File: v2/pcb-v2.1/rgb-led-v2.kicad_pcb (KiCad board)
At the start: 2 copper layers, 90 x 50 mm, 12 parts, among them SW1 SPST

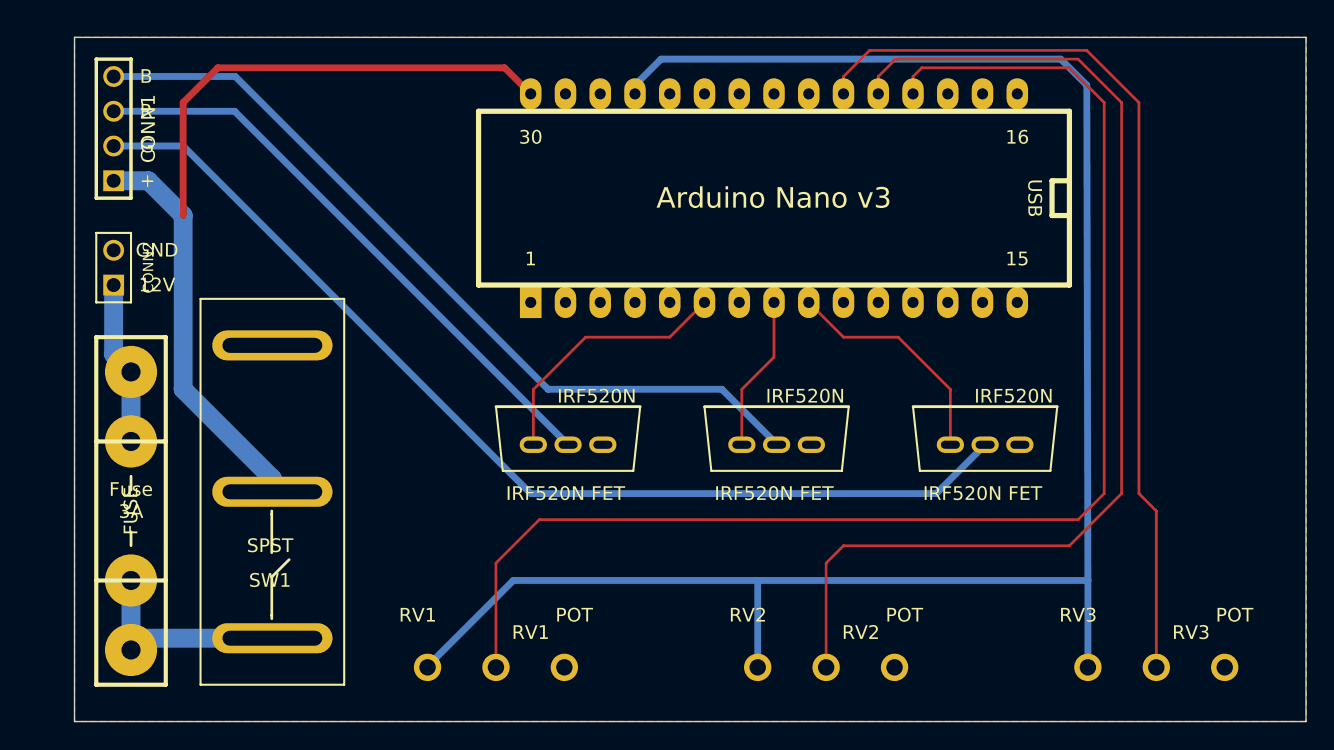
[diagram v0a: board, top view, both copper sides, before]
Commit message: Add DC jack
Fixes #1
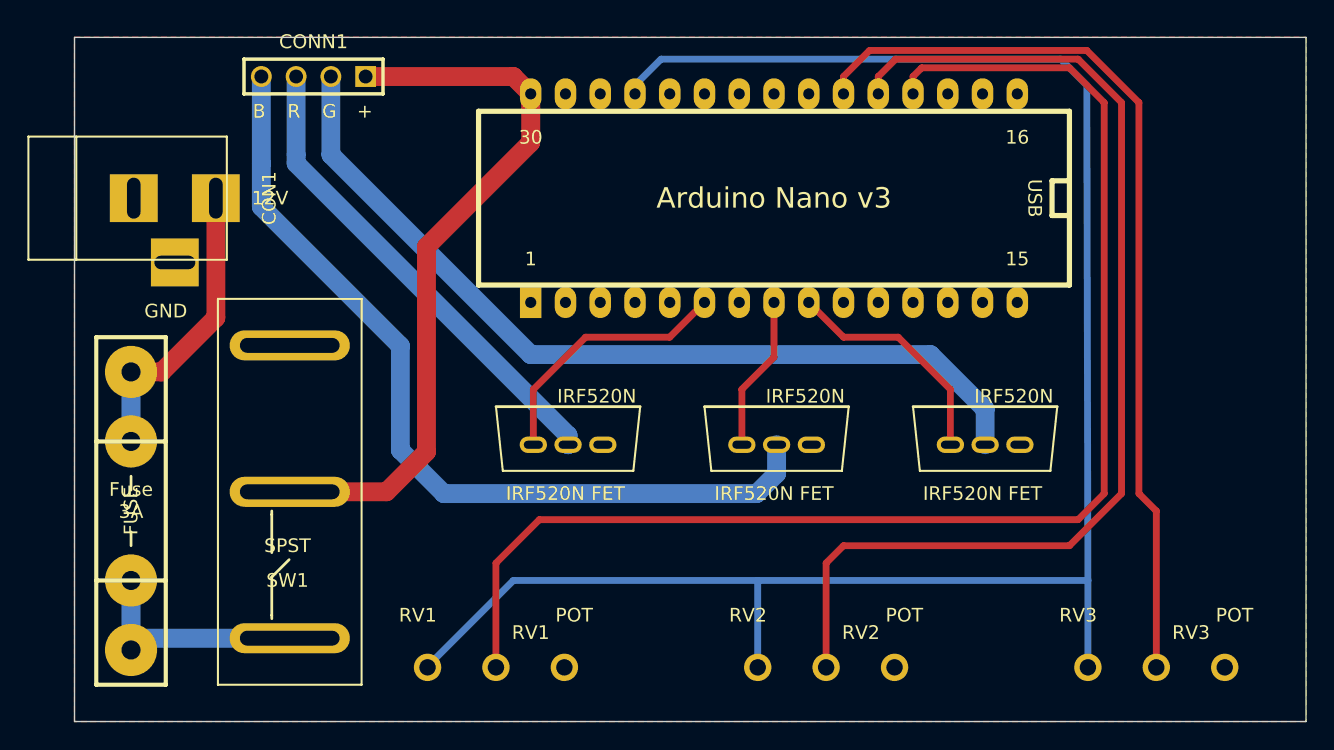
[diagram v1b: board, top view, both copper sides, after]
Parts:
- removed CONN2: VCC 12V, PIN_ARRAY_2X1
- added CON1: BARREL_JACK, Connect:BARREL_JACK, F.Cu at (22.9, 31.8)
- moved CONN1 15.1 mm to (36.2, 22.9), turned to 180 degrees
- moved SW1 1.27 mm to (29.2, 67.3)
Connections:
- UC1 pad 1: (no net) -> Net-(UC1-Pad1)
- UC1 pad 10: (no net) -> Net-(UC1-Pad10)
- UC1 pad 11: (no net) -> Net-(UC1-Pad11)
- UC1 pad 13: (no net) -> Net-(UC1-Pad13)
- UC1 pad 16: (no net) -> Net-(UC1-Pad16)
- UC1 pad 17: (no net) -> Net-(UC1-Pad17)
- UC1 pad 18: (no net) -> Net-(UC1-Pad18)
- UC1 pad 2: (no net) -> Net-(UC1-Pad2)
- UC1 pad 20: (no net) -> Net-(UC1-Pad20)
- UC1 pad 22: (no net) -> Net-(UC1-Pad22)
- UC1 pad 25: (no net) -> Net-(UC1-Pad25)
- UC1 pad 26: (no net) -> Net-(UC1-Pad26)
- UC1 pad 27: (no net) -> Net-(UC1-Pad27)
- UC1 pad 28: (no net) -> Net-(UC1-Pad28)
- UC1 pad 29: (no net) -> Net-(UC1-Pad29)
- UC1 pad 3: (no net) -> Net-(UC1-Pad3)
- UC1 pad 30: (no net) -> Net-(UC1-Pad30)
- UC1 pad 7: (no net) -> Net-(UC1-Pad7)
- UC1 pad 8: (no net) -> Net-(UC1-Pad8)
- UC1 pad 9: (no net) -> Net-(UC1-Pad9)
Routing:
- net Net-(CONN1-Pad2): track 75.7 -> 63.9 mm
- net Net-(CONN1-Pad1): track 64.5 -> 53.1 mm, vias 2 -> 0
- net Net-(CON1-Pad1): track 12.0 -> 21.7 mm
- net Net-(CONN1-Pad3): track 43.4 -> 35.2 mm
- net Net-(CONN1-Pad4): track 59.6 -> 63.1 mm

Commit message: Move open hardware logo and improve spacing
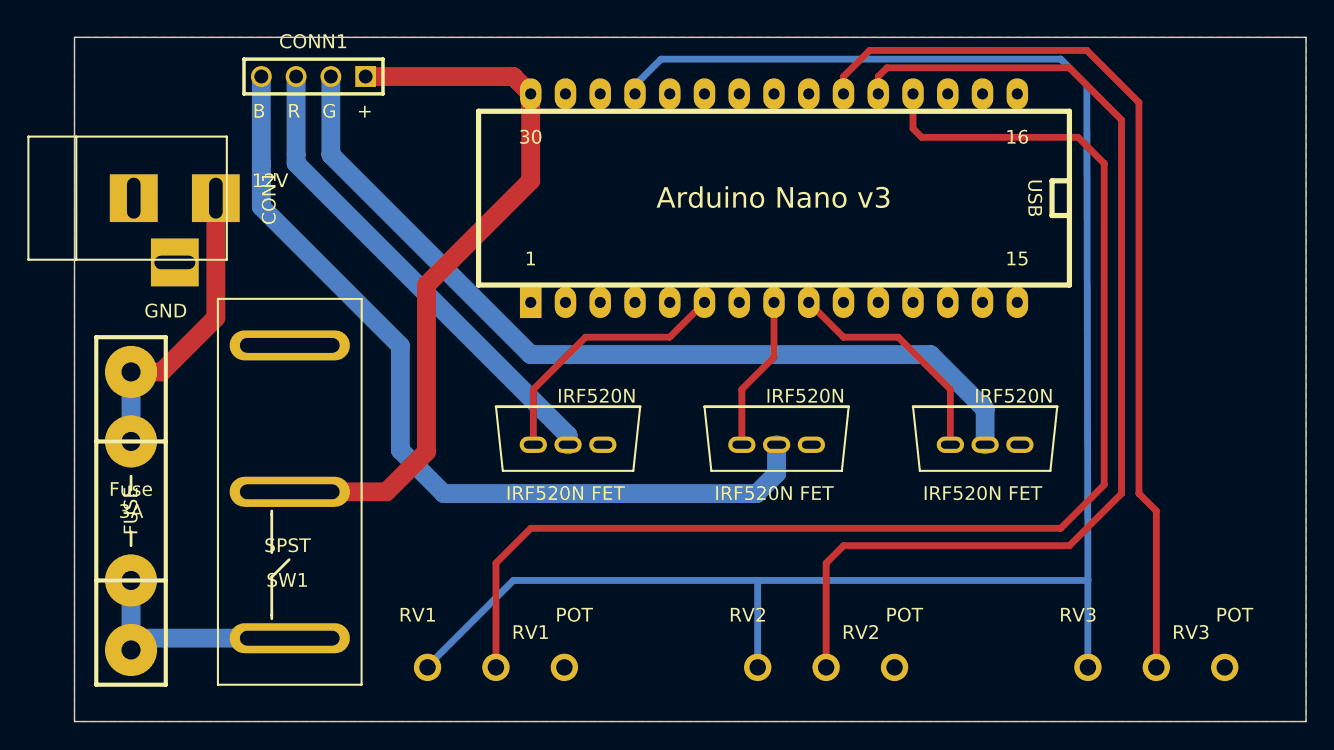
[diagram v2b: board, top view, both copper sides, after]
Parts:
- moved G*** 2.01 mm to (38.7, 29.2)
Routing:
- net Net-(RV1-Pad2): track 99.3 -> 95.5 mm
- net Net-(RV2-Pad2): track 80.8 -> 79.5 mm
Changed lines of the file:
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@@
     (links 27)
     (no_connects 0)
-    (area 18.679999 19.949999 108.780001 70.050001)
+    (area 15.269379 19.4922 108.780001 70.050001)
     (thickness 1.6)
     (drawings 35)
@@
   (layers
     (0 F.Cu signal)
-    (31 B.Cu signal)
+    (31 B.Cu signal hide)
     (32 B.Adhes user)
     (33 F.Adhes user)
@@
   )
   (module OSHW_MASK_7MM (layer F.Cu)
-    (at 36.83 28.575)
+    (at 38.735 29.21)
     (fp_text reference G*** (at 0 3.71094) (layer F.Mask) hide
       (effects (font (size 0.3175 0.3175) (thickness 0.0635)))
@@
     (effects (font (size 1 1) (thickness 0.15)))
   )
-  (gr_text 12V (at 33.02 31.75) (layer F.SilkS)
+  (gr_text 12V (at 33.02 30.48) (layer F.SilkS)
     (effects (font (size 1 1) (thickness 0.15)))
   )
@@
     (effects (font (size 1 1) (thickness 0.15)))
   )
-  (gr_text "open source\nhardware" (at 36.83 33.655) (layer F.Mask)
+  (gr_text "open source\nhardware" (at 38.735 34.29) (layer F.Mask)
     (effects (font (size 1.4 1.4) (thickness 0.25)))
   )
@@
   (segment (start 29.06014 40.49014) (end 25.10028 44.45) (width 1.38) (layer F.Cu) (net 2))
   (segment (start 22.86 44.45) (end 22.86 49.53) (width 1.38) (layer B.Cu) (net 2) (status 30))
+  (segment (start 44.45 38.1) (end 52.07 30.48) (width 1.38) (layer F.Cu) (net 3))
+  (segment (start 52.07 30.48) (end 52.07 24.13) (width 1.38) (layer F.Cu) (net 3))
   (segment (start 40.005 22.86) (end 50.8 22.86) (width 1.38) (layer F.Cu) (net 3) (status 10))
   (segment (start 50.8 22.86) (end 52.07 24.13) (width 1.38) (layer F.Cu) (net 3) (status 20))
-  (segment (start 52.07 24.13) (end 52.07 27.686) (width 1.38) (layer F.Cu) (net 3) (status 10))
   (segment (start 41.532 53.21) (end 34.46 53.21) (width 1.38) (layer F.Cu) (net 3) (status 20))
   (segment (start 44.45 50.292) (end 41.532 53.21) (width 1.38) (layer F.Cu) (net 3))
-  (segment (start 44.45 35.306) (end 44.45 50.292) (width 1.38) (layer F.Cu) (net 3))
-  (segment (start 52.07 27.686) (end 44.45 35.306) (width 1.38) (layer F.Cu) (net 3))
+  (segment (start 44.45 38.1) (end 44.45 50.292) (width 1.38) (layer F.Cu) (net 3))
   (segment (start 37.465 22.86) (end 37.465 28.575) (width 1.38) (layer B.Cu) (net 4) (status 10))
   (segment (start 37.465 28.575) (end 52.07 43.18) (width 1.38) (layer B.Cu) (net 4))
@@
   (segment (start 92.71 23.495) (end 92.79 59.69) (width 0.5) (layer B.Cu) (net 11))
   (segment (start 92.79 59.69) (end 92.79 66.04) (width 0.5) (layer B.Cu) (net 11) (status 20))
-  (segment (start 80.01 24.13) (end 80.01 22.86) (width 0.5) (layer F.Cu) (net 12) (status 10))
+  (segment (start 93.98 52.705) (end 90.805 55.88) (width 0.5) (layer F.Cu) (net 12))
+  (segment (start 90.805 55.88) (end 52.07 55.88) (width 0.5) (layer F.Cu) (net 12))
+  (segment (start 80.01 24.13) (end 80.01 26.67) (width 0.5) (layer F.Cu) (net 12))
+  (segment (start 92.075 27.305) (end 93.98 29.21) (width 0.5) (layer F.Cu) (net 12))
+  (segment (start 80.645 27.305) (end 92.075 27.305) (width 0.5) (layer F.Cu) (net 12))
+  (segment (start 80.01 26.67) (end 80.645 27.305) (width 0.5) (layer F.Cu) (net 12))
+  (segment (start 93.98 29.21) (end 93.98 52.705) (width 0.5) (layer F.Cu) (net 12))
   (segment (start 49.53 58.42) (end 49.53 66.04) (width 0.5) (layer F.Cu) (net 12) (status 20))
-  (segment (start 52.705 55.245) (end 49.53 58.42) (width 0.5) (layer F.Cu) (net 12))
-  (segment (start 92.075 55.245) (end 52.705 55.245) (width 0.5) (layer F.Cu) (net 12))
-  (segment (start 93.98 53.34) (end 92.075 55.245) (width 0.5) (layer F.Cu) (net 12))
-  (segment (start 93.98 24.765) (end 93.98 53.34) (width 0.5) (layer F.Cu) (net 12))
-  (segment (start 91.44 22.225) (end 93.98 24.765) (width 0.5) (layer F.Cu) (net 12))
-  (segment (start 80.645 22.225) (end 91.44 22.225) (width 0.5) (layer F.Cu) (net 12))
-  (segment (start 80.01 22.86) (end 80.645 22.225) (width 0.5) (layer F.Cu) (net 12))
-  (segment (start 77.47 24.13) (end 77.47 22.86) (width 0.5) (layer F.Cu) (net 13) (status 10))
+  (segment (start 52.07 55.88) (end 49.53 58.42) (width 0.5) (layer F.Cu) (net 12))
+  (segment (start 77.47 24.13) (end 77.47 22.86) (width 0.5) (layer F.Cu) (net 13))
+  (segment (start 77.47 22.86) (end 78.105 22.225) (width 0.5) (layer F.Cu) (net 13))
+  (segment (start 91.44 22.225) (end 95.25 26.035) (width 0.5) (layer F.Cu) (net 13))
+  (segment (start 78.105 22.225) (end 91.44 22.225) (width 0.5) (layer F.Cu) (net 13))
   (segment (start 73.66 58.42) (end 73.66 66.04) (width 0.5) (layer F.Cu) (net 13) (status 20))
   (segment (start 74.93 57.15) (end 73.66 58.42) (width 0.5) (layer F.Cu) (net 13))
   (segment (start 91.44 57.15) (end 74.93 57.15) (width 0.5) (layer F.Cu) (net 13))
   (segment (start 95.25 53.34) (end 91.44 57.15) (width 0.5) (layer F.Cu) (net 13))
-  (segment (start 95.25 24.765) (end 95.25 53.34) (width 0.5) (layer F.Cu) (net 13))
-  (segment (start 92.075 21.59) (end 95.25 24.765) (width 0.5) (layer F.Cu) (net 13))
-  (segment (start 78.74 21.59) (end 92.075 21.59) (width 0.5) (layer F.Cu) (net 13))
-  (segment (start 77.47 22.86) (end 78.74 21.59) (width 0.5) (layer F.Cu) (net 13))
+  (segment (start 95.25 26.035) (end 95.25 53.34) (width 0.5) (layer F.Cu) (net 13))
   (segment (start 74.93 24.13) (end 74.93 22.86) (width 0.5) (layer F.Cu) (net 14) (status 10))
   (segment (start 97.79 54.61) (end 97.79 66.04) (width 0.5) (layer F.Cu) (net 14) (status 20))

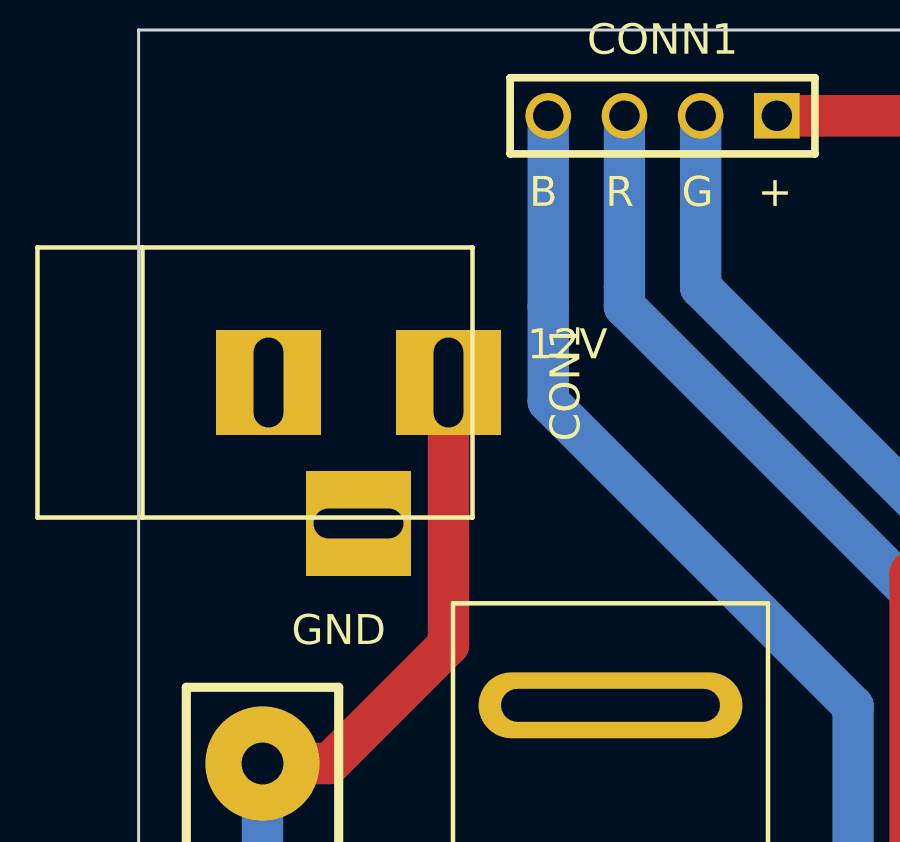
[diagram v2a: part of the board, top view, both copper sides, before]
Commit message: Update metadata and text label
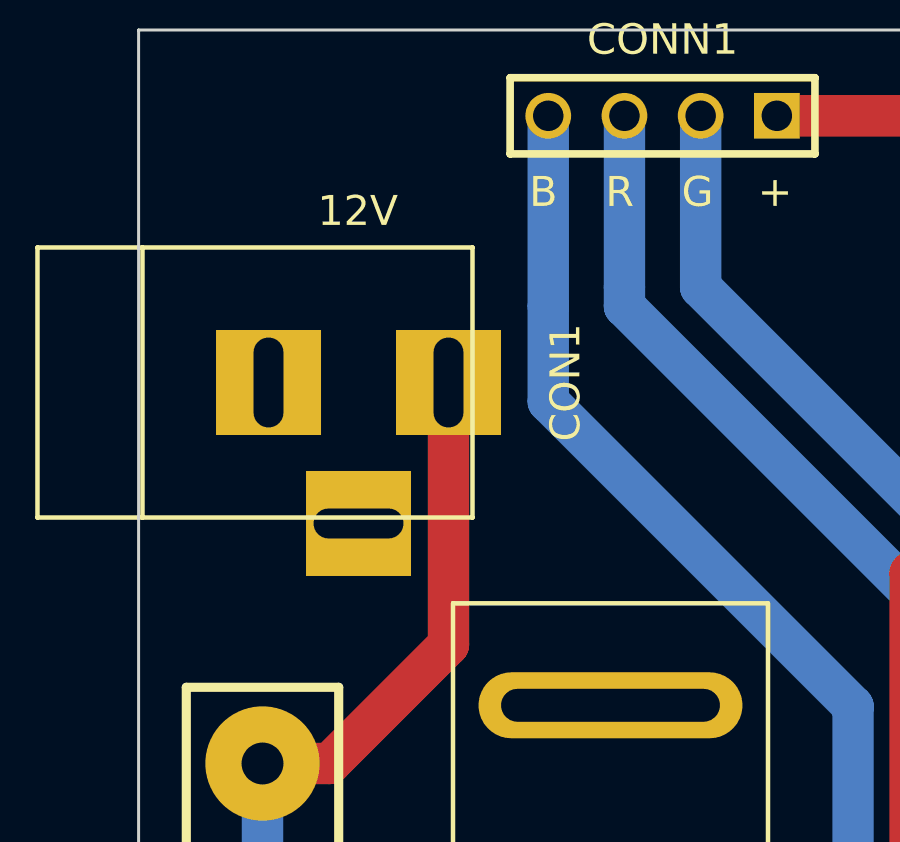
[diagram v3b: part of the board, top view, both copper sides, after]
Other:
- board text added: "coredump RGB LED V2.1 2016"
- board text removed: "GND"
- board text removed: "coredump RGB LED V2 2014"
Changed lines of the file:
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@@
     (area 15.269379 19.4922 108.780001 70.050001)
     (thickness 1.6)
-    (drawings 35)
+    (drawings 34)
     (tracks 83)
     (zones 0)
@@
   )
   (setup
-    (last_trace_width 1.38)
+    (last_trace_width 0.01)
     (user_trace_width 0.2)
     (user_trace_width 0.5)
@@
     (effects (font (size 1 1) (thickness 0.15)) (justify left))
   )
-  (gr_text GND (at 25.4 40.005) (layer F.SilkS)
-    (effects (font (size 1 1) (thickness 0.15)))
-  )
-  (gr_text 12V (at 33.02 30.48) (layer F.SilkS)
+  (gr_text 12V (at 26.035 26.035) (layer F.SilkS)
     (effects (font (size 1 1) (thickness 0.15)))
   )
@@
     (effects (font (size 1.4 1.4) (thickness 0.25)))
   )
-  (gr_text "coredump\nRGB LED V2 2014" (at 104.775 36.83 270) (layer F.Mask)
+  (gr_text "coredump\nRGB LED V2.1 2016" (at 104.14 43.18 270) (layer F.Mask)
     (effects (font (size 2 2) (thickness 0.3)))
   )
